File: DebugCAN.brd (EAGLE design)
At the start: 64 x 57 mm, 56 parts, among them J1 8P8C-LED, J3 MA04-1, J4 10118192-0001LF, J5 8P8C-LED, J6 8P8C-LED, J7 8P8C-LED, U1 STM32F302C, U2 NCV7351D1E, U3 SI8621AB-B-IS, U4 AP2127N-3.3TRG1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

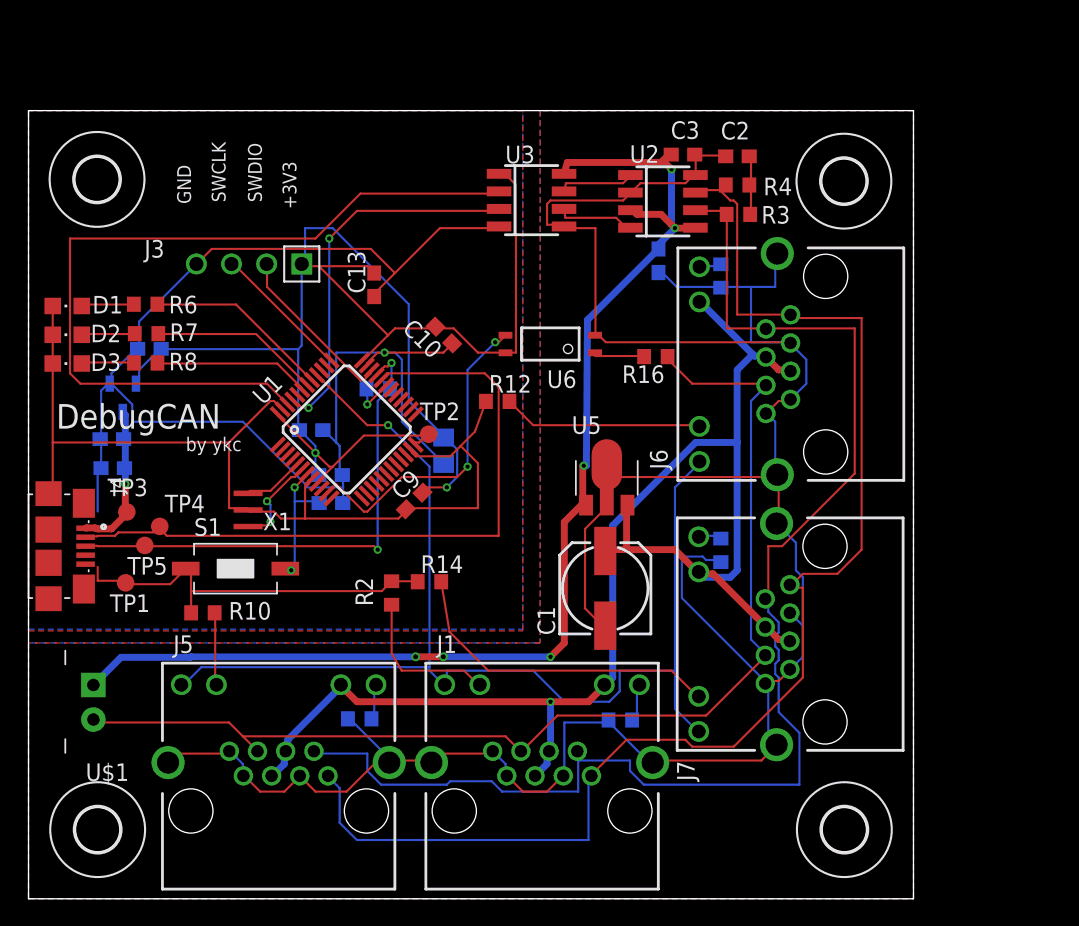
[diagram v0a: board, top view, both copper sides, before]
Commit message: NUC電源の管理を追加
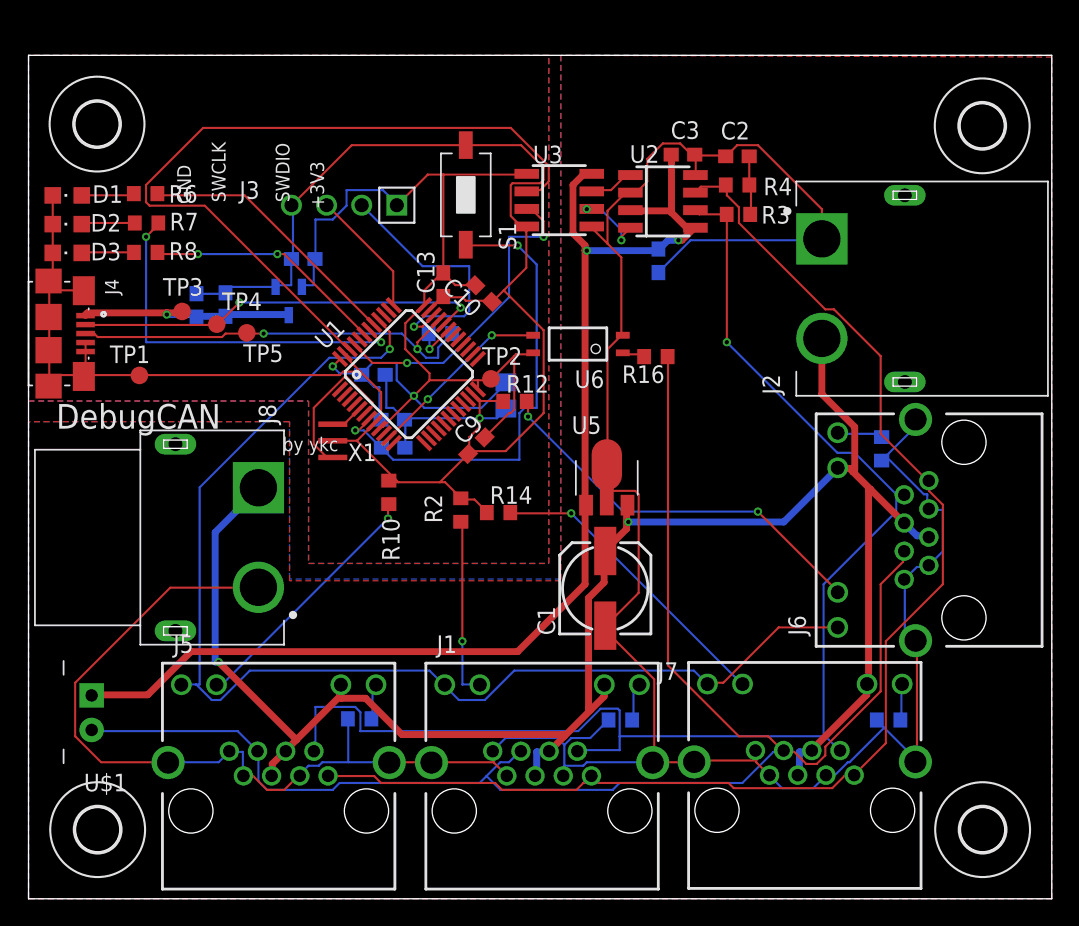
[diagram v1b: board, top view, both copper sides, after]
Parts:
- added J2: XT60PW-M, con-xt:AMASS_XT60PW-M
- added J8: XT60PW-F, con-xt:AMASS_XT60PW-F
- moved S1 31.7 mm to (31.6, 50.9), turned to 270 degrees
- moved R13 17.3 mm to (62.2, 12.9), turned to 180 degrees
- moved R11 17.1 mm to (61.7, 32.5)
- moved TP5 17.1 mm to (15.8, 40.9)
- moved R10 16.0 mm to (26.1, 29.4), turned to 270 degrees
- moved J6 15.6 mm to (61.3, 26.7)
- moved J4 15.4 mm to (4.12, 40.9)
- moved TP4 15.2 mm to (13.6, 41.6)
- moved TP3 15.0 mm to (11.1, 42.5)
- moved TP1 15.0 mm to (8.02, 37.9)
- moved U4 13.9 mm to (18.8, 43.2)
- moved C6 13.2 mm to (12.1, 42.9), turned to 90 degrees
- moved C8 12.9 mm to (19.9, 46.3)
- moved C5 12.7 mm to (14.2, 43.0), turned to 90 degrees
- moved H1 10.8 mm to (69.0, 55.9)
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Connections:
- net +12V: now also J2.2, J8.2
- net GNDIO: now also J2.1, J8.1
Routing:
- net GNDA: track 201.9 -> 160.4 mm
- net EMS: track 82.5 -> 112.4 mm
- net +3V3: track 114.3 -> 85.4 mm
- net +12V: track 105.5 -> 133.0 mm, vias 1 -> 2
- net !RESET: track 9.79 -> 35.1 mm
- net GNDIO: track 198.6 -> 220.6 mm
- net USB_DM: track 50.4 -> 29.8 mm, vias 0 -> 2
- net LED1: track 12.3 -> 27.3 mm, vias 0 -> 2
- net N$13: track 14.5 -> 28.8 mm, vias 0 -> 2
- net N$10: track 5.28 -> 18.5 mm, vias 0 -> 1
- net !EMS: track 23.4 -> 13.5 mm
- net SWDIO: track 12.4 -> 19.1 mm, vias 0 -> 1
- net LED0: track 13.4 -> 19.6 mm
- net LED2: track 11.3 -> 17.5 mm, vias 0 -> 2
- net USB_DP: track 36.7 -> 31.4 mm
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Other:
- board size 64 x 57 mm -> 74 x 61 mm

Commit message: 微修正
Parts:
- moved H1 0.80 mm to (68.5, 56.5)
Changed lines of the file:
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@@
 <attribute name="VALUE" x="4.07" y="49.25" size="1.27" layer="27" rot="R180"/>
 </element>
-<element name="H1" library="holes" library_urn="urn:adsk.eagle:library:237" package="3,2" package3d_urn="urn:adsk.eagle:package:14275/1" value="MOUNT-HOLE3.2" x="68.97" y="55.9" smashed="yes"/>
+<element name="H1" library="holes" library_urn="urn:adsk.eagle:library:237" package="3,2" package3d_urn="urn:adsk.eagle:package:14275/1" value="MOUNT-HOLE3.2" x="68.47" y="56.525" smashed="yes"/>
 <element name="H2" library="holes" library_urn="urn:adsk.eagle:library:237" package="3,2" package3d_urn="urn:adsk.eagle:package:14275/1" value="MOUNT-HOLE3.2" x="4.955" y="56.025" smashed="yes"/>
 <element name="J1" library="con-rj45" package="8P8C-LED" value="8P8C-LED" x="37.14" y="12.7" smashed="yes">

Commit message: fainal version
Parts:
- removed J2: XT60PW-M, con-xt:AMASS_XT60PW-M
- moved R13 16.4 mm to (52.2, 25.9), turned to 90 degrees
- moved R11 15.6 mm to (51.7, 44.5)
- moved J6 14.5 mm to (52.4, 38.2)
- moved H4 9.00 mm to (60.0, 5.00)
- moved H1 8.00 mm to (60.5, 56.5)
- moved J7 7.74 mm to (52.4, 19.5), turned to 90 degrees
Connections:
- net +12V: no longer J2.2
- net GNDIO: no longer J2.1
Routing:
- net CANTX: track 55.4 -> 23.7 mm, vias 0 -> 2
- net EMS: track 112.4 -> 86.6 mm
- net GNDIO: track 220.6 -> 198.9 mm
- net +12V: track 133.0 -> 112.5 mm, vias 2 -> 0
- net CANL: track 99.1 -> 80.7 mm, vias 1 -> 2
- net N$13: track 28.8 -> 14.6 mm, vias 2 -> 0
- net GNDA: track 160.4 -> 171.9 mm, vias 1 -> 3
- net CANH: track 94.7 -> 83.7 mm
- net LED1: track 27.3 -> 18.5 mm, vias 2 -> 0
- net CAN_LED: track 87.6 -> 96.1 mm
- net !RESET: track 35.1 -> 27.2 mm
- net SWDIO: track 19.1 -> 11.4 mm, vias 1 -> 0
- net CANRX: track 23.3 -> 17.0 mm
- net +5V_ISO: track 88.1 -> 92.4 mm, vias 2 -> 4
- net N$7: track 11.5 -> 14.0 mm, vias 0 -> 2
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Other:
- board size 74 x 61 mm -> 65 x 61 mm
- board text added: "ver NHK2024"

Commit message: renew position
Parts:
- removed J8: XT60PW-F, con-xt:AMASS_XT60PW-F
- added J2: XT60PW-M, con-xt:AMASS_XT60PW-M
- C3, C4: value (none) -> 100n
- D1: value (none) -> GREEN
- D2: value (none) -> YELLOW
- D3: value (none) -> RED
- R1, R11, R13, R9: value (none) -> 1k
- R10, R12, R14, R2: value (none) -> 470
- moved D3 50.8 mm to (53.5, 50.9), turned to 270 degrees
- moved D1 50.8 mm to (53.5, 46.8), turned to 270 degrees
- moved D2 50.7 mm to (53.5, 48.8), turned to 270 degrees
- moved J4 47.8 mm to (51.9, 40.9), turned to 90 degrees
- moved U$1 47.7 mm to (51.5, 12.8), turned to 180 degrees
- moved R11 43.2 mm to (17.3, 18.5), turned to 270 degrees
- moved TP1 42.6 mm to (50.0, 44.9)
- moved J6 41.7 mm to (12.6, 25.8), turned to 270 degrees
- moved R6 39.6 mm to (47.8, 46.6), turned to 0 degrees
- moved R8 39.5 mm to (47.8, 50.9), turned to 0 degrees
- moved R7 39.2 mm to (47.7, 48.8), turned to 0 degrees
- moved C3 38.2 mm to (28.7, 20.5), turned to 90 degrees
- moved C6 37.6 mm to (49.4, 37.2), turned to 270 degrees
- moved R3 37.6 mm to (14.6, 57.6)
- moved R4 37.6 mm to (14.5, 59.7)
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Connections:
- net +12V: now also J2.2; no longer J8.2
- net GNDIO: now also J2.1; no longer J8.1
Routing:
- net GNDIO: track 198.9 -> 0.00 mm, vias 0 -> 4
- net GNDA: track 171.9 -> 0.00 mm, vias 3 -> 23
- net EMS: track 86.6 -> 130.3 mm
- net CANL: track 80.7 -> 106.9 mm, vias 2 -> 1
- net CANH: track 83.7 -> 107.2 mm, vias 0 -> 1
- net N$4: track 13.1 -> 35.0 mm, vias 0 -> 1
- net USB_DP: track 32.6 -> 12.6 mm, vias 2 -> 0
- net USB_DM: track 29.1 -> 11.8 mm, vias 2 -> 0
- net N$10: track 18.2 -> 7.68 mm
- net N$7: track 14.0 -> 3.97 mm, vias 2 -> 0
- net CAN_LED: track 96.1 -> 104.9 mm, vias 1 -> 0
- net !EMS: track 13.5 -> 5.60 mm, vias 2 -> 0
- net LED2: track 17.5 -> 24.4 mm
- net LED1: track 18.5 -> 25.3 mm
- net N$15: track 23.4 -> 30.1 mm, vias 0 -> 1
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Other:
- board size 65 x 61 mm -> 56 x 63 mm
- board text added: "ver NHK2024-Ⅱ"
- board text removed: "ver NHK2024"
